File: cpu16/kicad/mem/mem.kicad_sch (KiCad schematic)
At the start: 16 parts, among them J2 BACKPLANE_2x32, U116 74HC688, U117 74HC688, U118 62256, U119 62256, U120 74HC574, U135 74HC32, U153 74HC04

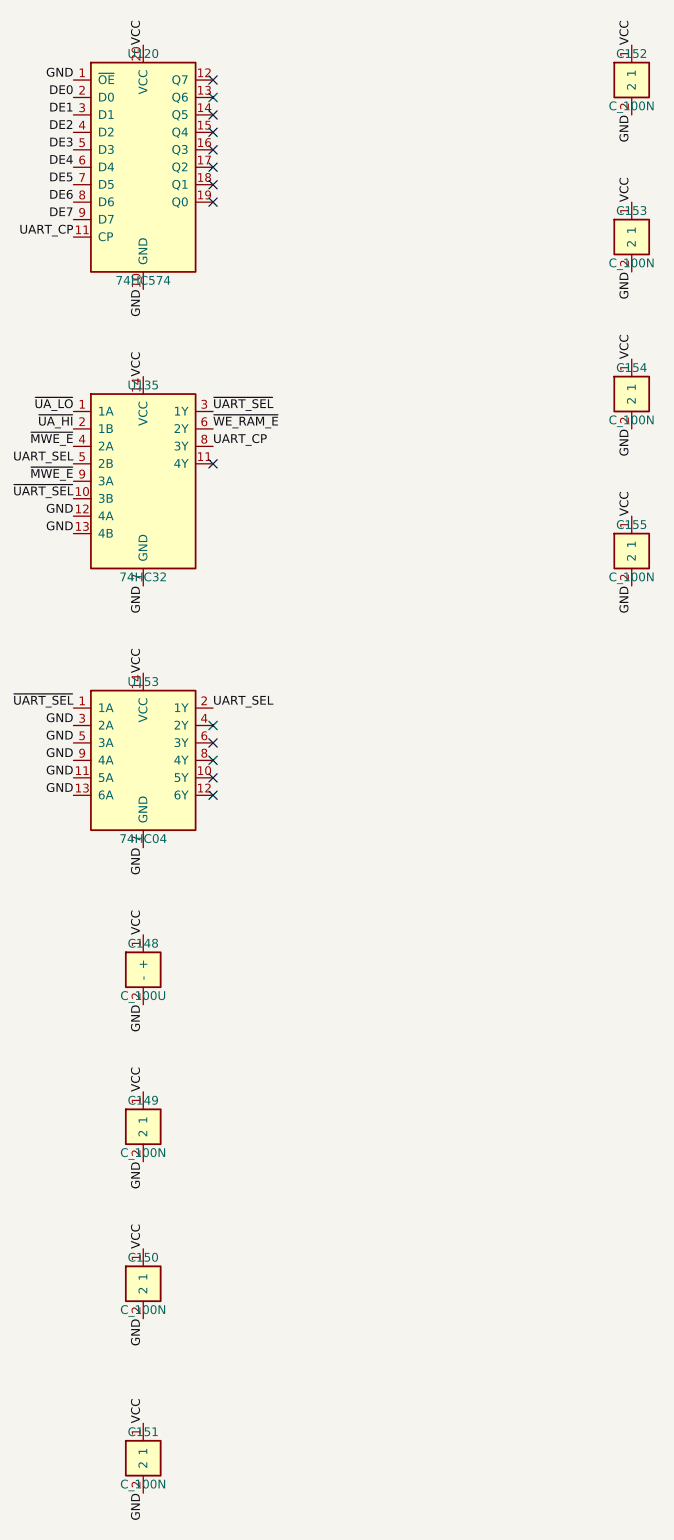
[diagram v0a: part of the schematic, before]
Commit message: CPU16 Faz 9 (1): saat/reset kartı, Flash programlayıcı ve ROM imajları
- Saat ve reset kartı (9 entegre): kristal / yavaş RC osilatör seçimi, 8 durumlu Johnson sayacıyla
  parazitsiz CLK ve WR_WIN, açılış reseti, tek döngü ADIM butonu (eşzamanlı), saat sürücüsü.
  Kapı seviyesi bilgisayar artık yalnızca osilatörü sürer; bütün testler kartla birlikte geçer
- Flash programlayıcı: Arduino Nano yazılımı (Intel HEX, SST komut dizileri, DQ7 sorgulama,
  READ/SUM), yaz.py (pyserial), KiCad şeması ve BOM. Uçtan uca test: yazılımın kendisi derlenip
  kartın kapı seviyesi modeline (2 × 74HC595 + SST39SF010A) bağlanır
- cpu16/roms: mikrokod (4) ve ALU (3) Flash imajları, npm run cpu16 -- roms
- Board: çip başına footprint (ZIF soket), arka panelsiz kart, pasif referans çakışma denetimi

Co-Authored-By: Claude Opus 5.5 (1M context) <noreply@anthropic.com>
Claude-Session: https://claude.ai/code/session_018J8WVuECVRbQJyCbmF6Nsi
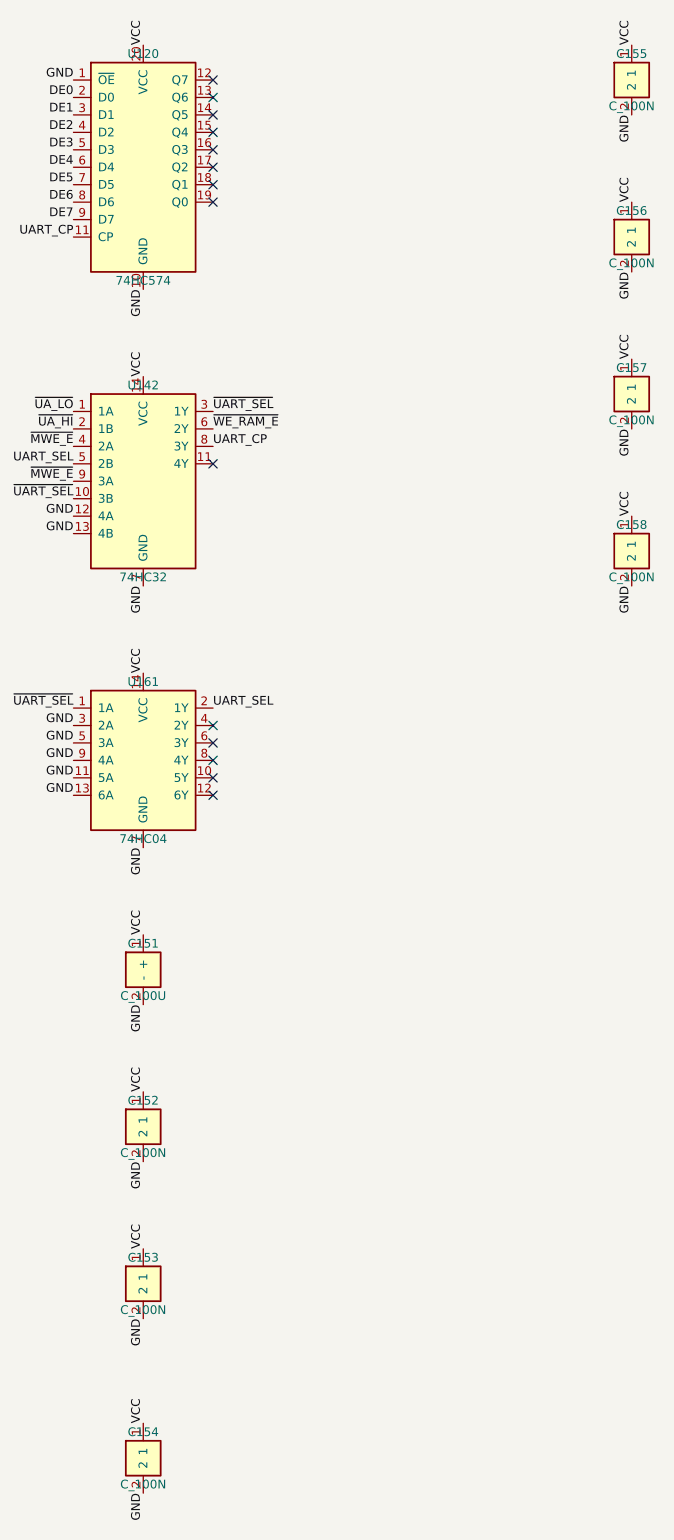
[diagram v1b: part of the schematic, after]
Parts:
- C157: renamed from C154; Gorev U135 dekuplaj -> U142 dekuplaj
- C158: renamed from C155; Gorev U153 dekuplaj -> U161 dekuplaj
- renumbered C148 to C151, C149 to C152, C150 to C153, C151 to C154, C152 to C155, C153 to C156, U135 to U142, U153 to U161
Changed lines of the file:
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@@
   (symbol (lib_id "cpu16:74HC32") (at 195.58 111.76 0) (unit 1)
     (in_bom yes) (on_board yes) (dnp no)
-    (property "Reference" "U135" (at 195.58 97.79 0) (effects (font (size 1.27 1.27))))
+    (property "Reference" "U142" (at 195.58 97.79 0) (effects (font (size 1.27 1.27))))
     (property "Value" "74HC32" (at 195.58 125.73 0) (effects (font (size 1.27 1.27))))
     (property "Footprint" "Package_DIP:DIP-14_W7.62mm" (at 195.58 111.76 0) (effects (font (size 1.27 1.27)) hide))
@@
     (pin "13")
     (pin "14")
-    (instances (project "mem" (path "/2ef92f41-0000-4000-8000-000000000001" (reference "U135") (unit 1))))
+    (instances (project "mem" (path "/2ef92f41-0000-4000-8000-000000000001" (reference "U142") (unit 1))))
   )
   (symbol (lib_id "cpu16:74HC04") (at 195.58 152.4 0) (unit 1)
     (in_bom yes) (on_board yes) (dnp no)
-    (property "Reference" "U153" (at 195.58 140.97 0) (effects (font (size 1.27 1.27))))
+    (property "Reference" "U161" (at 195.58 140.97 0) (effects (font (size 1.27 1.27))))
     (property "Value" "74HC04" (at 195.58 163.83 0) (effects (font (size 1.27 1.27))))
     (property "Footprint" "Package_DIP:DIP-14_W7.62mm" (at 195.58 152.4 0) (effects (font (size 1.27 1.27)) hide))
@@
     (pin "13")
     (pin "14")
-    (instances (project "mem" (path "/2ef92f41-0000-4000-8000-000000000001" (reference "U153") (unit 1))))
+    (instances (project "mem" (path "/2ef92f41-0000-4000-8000-000000000001" (reference "U161") (unit 1))))
   )
   (symbol (lib_id "cpu16:C_100U") (at 195.58 182.88 0) (unit 1)
     (in_bom yes) (on_board yes) (dnp no)
-    (property "Reference" "C148" (at 195.58 179.07 0) (effects (font (size 1.27 1.27))))
+    (property "Reference" "C151" (at 195.58 179.07 0) (effects (font (size 1.27 1.27))))
     (property "Value" "C_100U" (at 195.58 186.69 0) (effects (font (size 1.27 1.27))))
     (property "Footprint" "Capacitor_THT:CP_Radial_D6.3mm_P2.50mm" (at 195.58 182.88 0) (effects (font (size 1.27 1.27)) hide))
@@
     (pin "1")
     (pin "2")
-    (instances (project "mem" (path "/2ef92f41-0000-4000-8000-000000000001" (reference "C148") (unit 1))))
+    (instances (project "mem" (path "/2ef92f41-0000-4000-8000-000000000001" (reference "C151") (unit 1))))
   )
   (symbol (lib_id "cpu16:C_100N") (at 195.58 205.74 0) (unit 1)
     (in_bom yes) (on_board yes) (dnp no)
-    (property "Reference" "C149" (at 195.58 201.93 0) (effects (font (size 1.27 1.27))))
+    (property "Reference" "C152" (at 195.58 201.93 0) (effects (font (size 1.27 1.27))))
     (property "Value" "C_100N" (at 195.58 209.55 0) (effects (font (size 1.27 1.27))))
     (property "Footprint" "Capacitor_THT:C_Disc_D5.0mm_W2.5mm_P5.00mm" (at 195.58 205.74 0) (effects (font (size 1.27 1.27)) hide))
@@
     (pin "1")
     (pin "2")
-    (instances (project "mem" (path "/2ef92f41-0000-4000-8000-000000000001" (reference "C149") (unit 1))))
+    (instances (project "mem" (path "/2ef92f41-0000-4000-8000-000000000001" (reference "C152") (unit 1))))
   )
   (symbol (lib_id "cpu16:C_100N") (at 195.58 228.6 0) (unit 1)
     (in_bom yes) (on_board yes) (dnp no)
-    (property "Reference" "C150" (at 195.58 224.79 0) (effects (font (size 1.27 1.27))))
+    (property "Reference" "C153" (at 195.58 224.79 0) (effects (font (size 1.27 1.27))))
     (property "Value" "C_100N" (at 195.58 232.41 0) (effects (font (size 1.27 1.27))))
     (property "Footprint" "Capacitor_THT:C_Disc_D5.0mm_W2.5mm_P5.00mm" (at 195.58 228.6 0) (effects (font (size 1.27 1.27)) hide))
@@
     (pin "1")
     (pin "2")
-    (instances (project "mem" (path "/2ef92f41-0000-4000-8000-000000000001" (reference "C150") (unit 1))))
+    (instances (project "mem" (path "/2ef92f41-0000-4000-8000-000000000001" (reference "C153") (unit 1))))
   )
   (symbol (lib_id "cpu16:C_100N") (at 195.58 254 0) (unit 1)
     (in_bom yes) (on_board yes) (dnp no)
-    (property "Reference" "C151" (at 195.58 250.19 0) (effects (font (size 1.27 1.27))))
+    (property "Reference" "C154" (at 195.58 250.19 0) (effects (font (size 1.27 1.27))))
     (property "Value" "C_100N" (at 195.58 257.81 0) (effects (font (size 1.27 1.27))))
     (property "Footprint" "Capacitor_THT:C_Disc_D5.0mm_W2.5mm_P5.00mm" (at 195.58 254 0) (effects (font (size 1.27 1.27)) hide))
@@
     (pin "1")
     (pin "2")
-    (instances (project "mem" (path "/2ef92f41-0000-4000-8000-000000000001" (reference "C151") (unit 1))))
+    (instances (project "mem" (path "/2ef92f41-0000-4000-8000-000000000001" (reference "C154") (unit 1))))
   )
   (symbol (lib_id "cpu16:C_100N") (at 266.7 53.34 0) (unit 1)
     (in_bom yes) (on_board yes) (dnp no)
-    (property "Reference" "C152" (at 266.7 49.53 0) (effects (font (size 1.27 1.27))))
+    (property "Reference" "C155" (at 266.7 49.53 0) (effects (font (size 1.27 1.27))))
     (property "Value" "C_100N" (at 266.7 57.15 0) (effects (font (size 1.27 1.27))))
     (property "Footprint" "Capacitor_THT:C_Disc_D5.0mm_W2.5mm_P5.00mm" (at 266.7 53.34 0) (effects (font (size 1.27 1.27)) hide))
@@
     (pin "1")
     (pin "2")
-    (instances (project "mem" (path "/2ef92f41-0000-4000-8000-000000000001" (reference "C152") (unit 1))))
+    (instances (project "mem" (path "/2ef92f41-0000-4000-8000-000000000001" (reference "C155") (unit 1))))
   )
   (symbol (lib_id "cpu16:C_100N") (at 266.7 76.2 0) (unit 1)
     (in_bom yes) (on_board yes) (dnp no)
-    (property "Reference" "C153" (at 266.7 72.39 0) (effects (font (size 1.27 1.27))))
+    (property "Reference" "C156" (at 266.7 72.39 0) (effects (font (size 1.27 1.27))))
     (property "Value" "C_100N" (at 266.7 80.01 0) (effects (font (size 1.27 1.27))))
     (property "Footprint" "Capacitor_THT:C_Disc_D5.0mm_W2.5mm_P5.00mm" (at 266.7 76.2 0) (effects (font (size 1.27 1.27)) hide))
@@
     (pin "1")
     (pin "2")
-    (instances (project "mem" (path "/2ef92f41-0000-4000-8000-000000000001" (reference "C153") (unit 1))))
+    (instances (project "mem" (path "/2ef92f41-0000-4000-8000-000000000001" (reference "C156") (unit 1))))
   )
   (symbol (lib_id "cpu16:C_100N") (at 266.7 99.06 0) (unit 1)
     (in_bom yes) (on_board yes) (dnp no)
-    (property "Reference" "C154" (at 266.7 95.25 0) (effects (font (size 1.27 1.27))))
+    (property "Reference" "C157" (at 266.7 95.25 0) (effects (font (size 1.27 1.27))))
     (property "Value" "C_100N" (at 266.7 102.87 0) (effects (font (size 1.27 1.27))))
     (property "Footprint" "Capacitor_THT:C_Disc_D5.0mm_W2.5mm_P5.00mm" (at 266.7 99.06 0) (effects (font (size 1.27 1.27)) hide))
     (property "Datasheet" "" (at 266.7 99.06 0) (effects (font (size 1.27 1.27)) hide))
-    (property "Gorev" "U135 dekuplaj" (at 266.7 99.06 0) (effects (font (size 1.27 1.27)) hide))
+    (property "Gorev" "U142 dekuplaj" (at 266.7 99.06 0) (effects (font (size 1.27 1.27)) hide))
     (pin "1")
     (pin "2")
-    (instances (project "mem" (path "/2ef92f41-0000-4000-8000-000000000001" (reference "C154") (unit 1))))
+    (instances (project "mem" (path "/2ef92f41-0000-4000-8000-000000000001" (reference "C157") (unit 1))))
   )
   (symbol (lib_id "cpu16:C_100N") (at 266.7 121.92 0) (unit 1)
     (in_bom yes) (on_board yes) (dnp no)
-    (property "Reference" "C155" (at 266.7 118.11 0) (effects (font (size 1.27 1.27))))
+    (property "Reference" "C158" (at 266.7 118.11 0) (effects (font (size 1.27 1.27))))
     (property "Value" "C_100N" (at 266.7 125.73 0) (effects (font (size 1.27 1.27))))
     (property "Footprint" "Capacitor_THT:C_Disc_D5.0mm_W2.5mm_P5.00mm" (at 266.7 121.92 0) (effects (font (size 1.27 1.27)) hide))
     (property "Datasheet" "" (at 266.7 121.92 0) (effects (font (size 1.27 1.27)) hide))
-    (property "Gorev" "U153 dekuplaj" (at 266.7 121.92 0) (effects (font (size 1.27 1.27)) hide))
+    (property "Gorev" "U161 dekuplaj" (at 266.7 121.92 0) (effects (font (size 1.27 1.27)) hide))
     (pin "1")
     (pin "2")
-    (instances (project "mem" (path "/2ef92f41-0000-4000-8000-000000000001" (reference "C155") (unit 1))))
+    (instances (project "mem" (path "/2ef92f41-0000-4000-8000-000000000001" (reference "C158") (unit 1))))
   )
   (label "GND" (at 45.72 53.34 180) (fields_autoplaced) (effects (font (size 1.27 1.27)) (justify right bottom)))
